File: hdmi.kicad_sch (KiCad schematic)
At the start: 25 parts, among them J3 HDMI_A, U3 TFP410PAP, U5 PCA9306, U6 TPS2041B

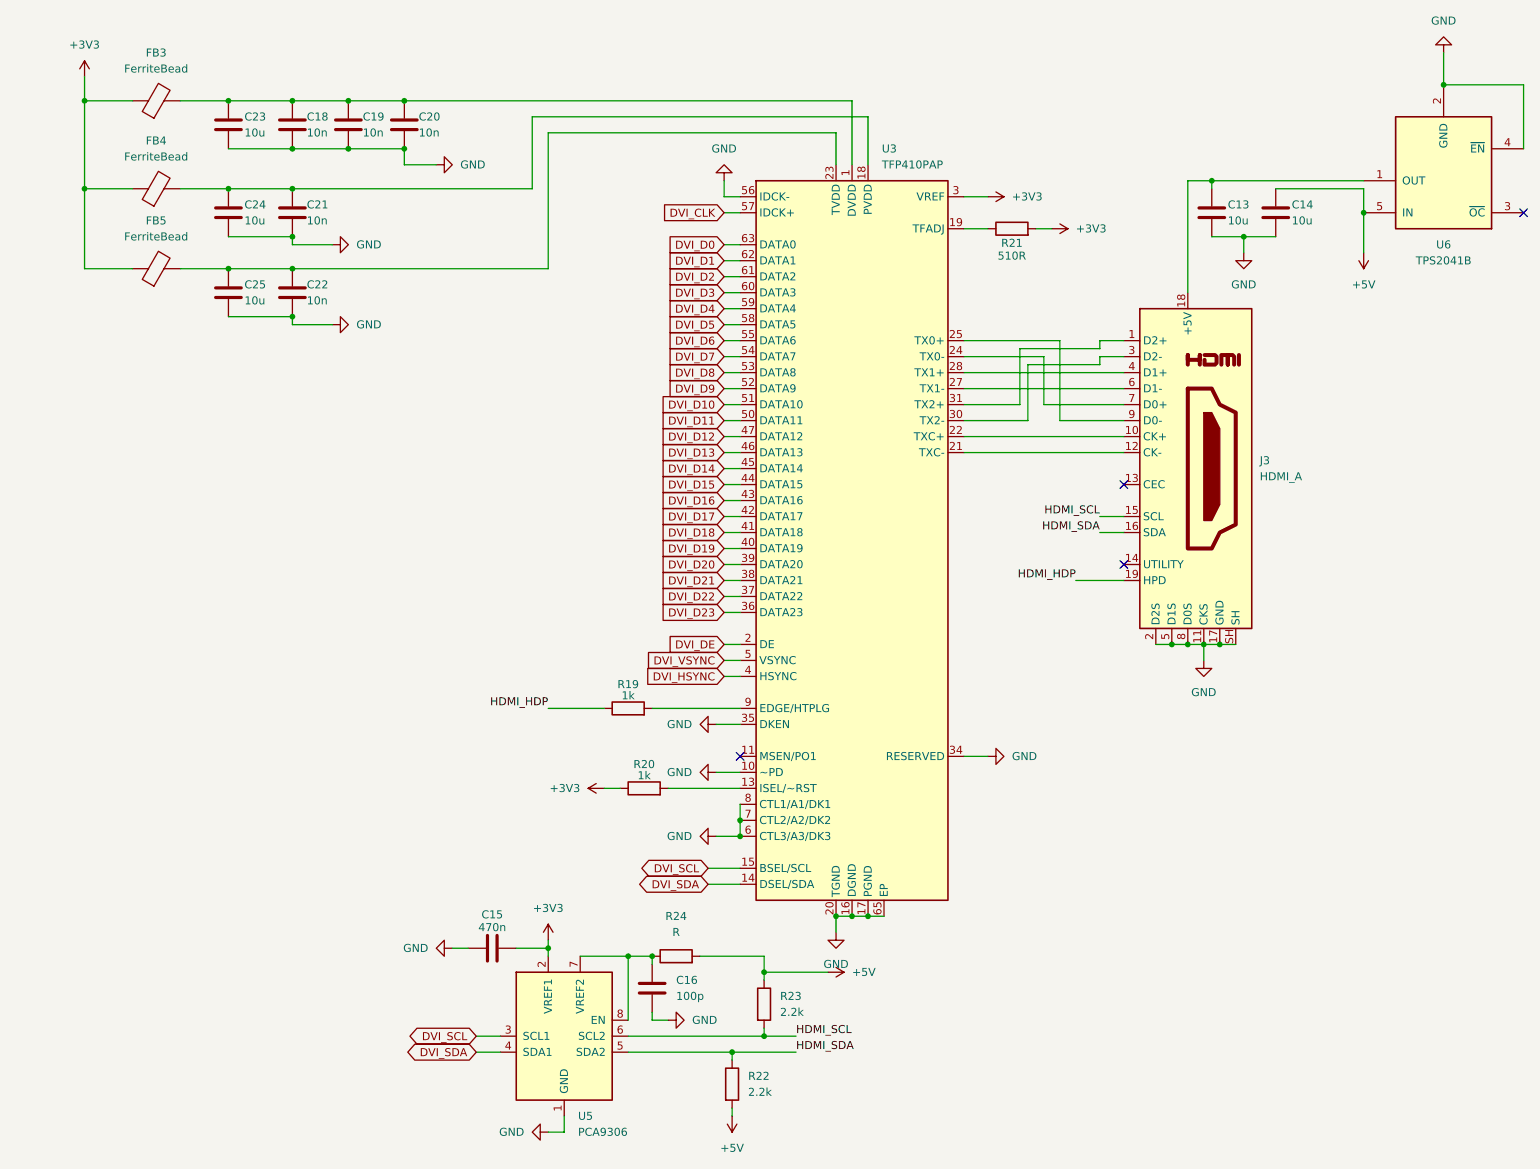
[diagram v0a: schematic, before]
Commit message: Adicionando novos datasheets e comecando power
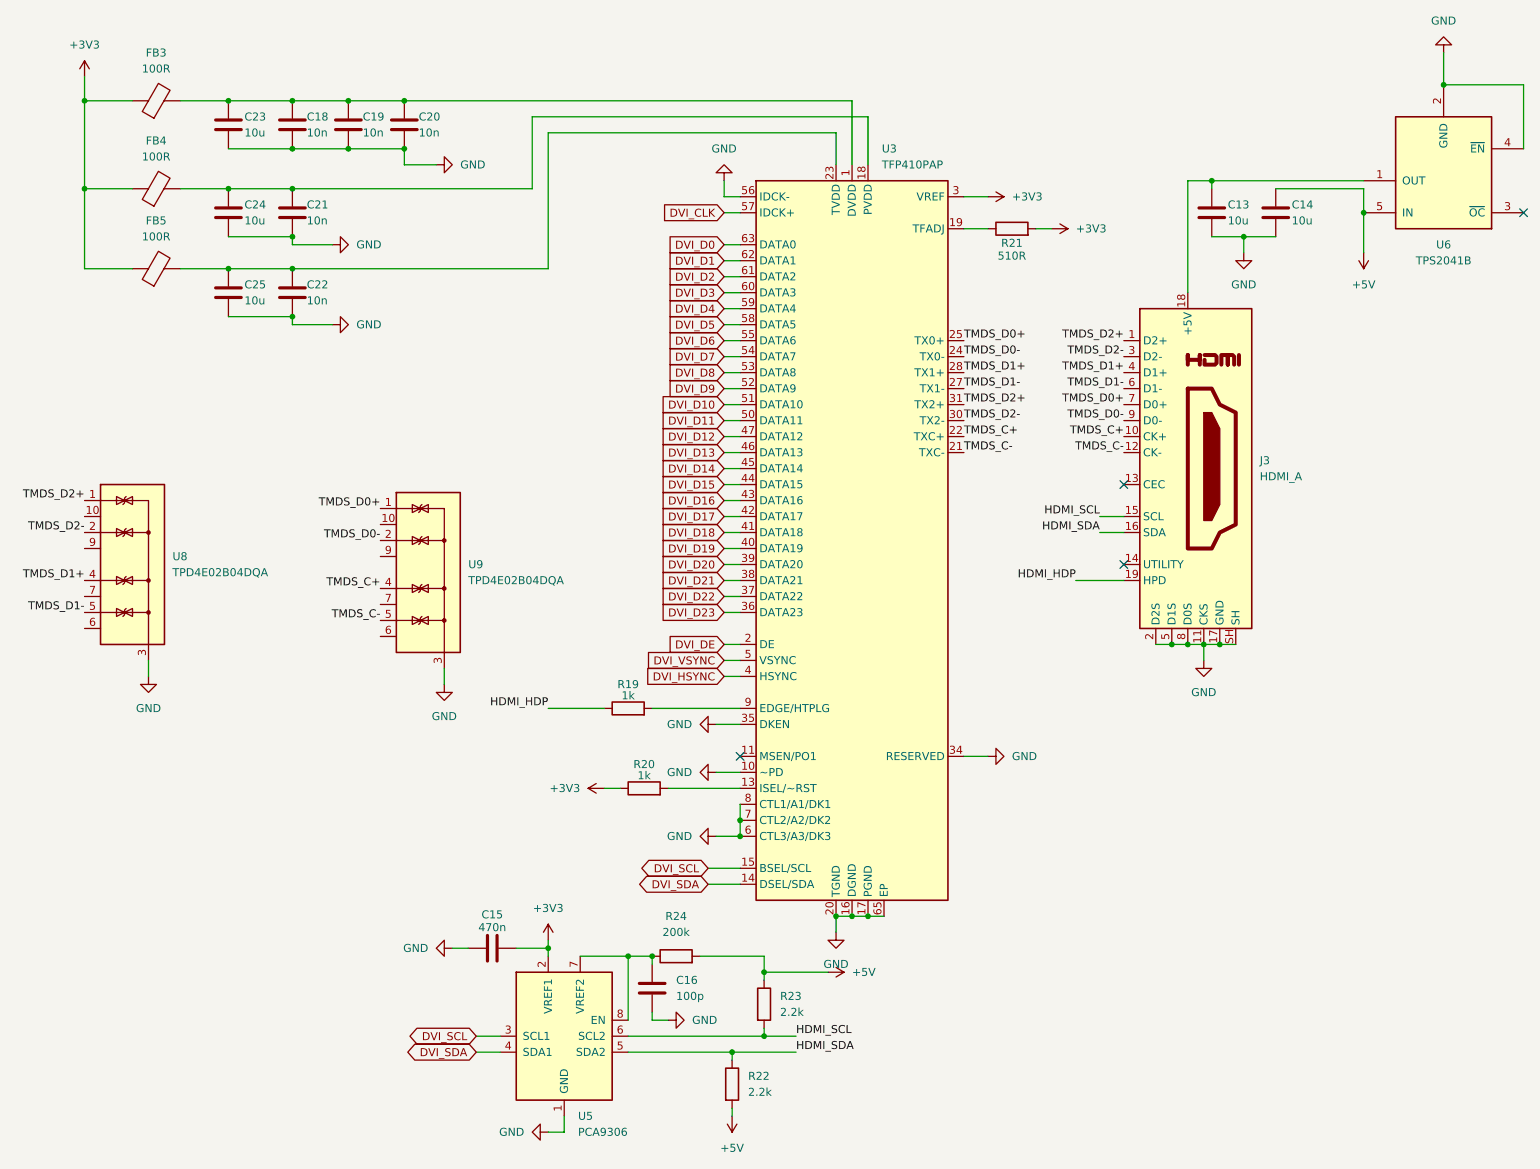
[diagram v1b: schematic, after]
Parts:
- added U8, U9: TPD4E02B04DQA, Package_SON:USON-10_2.5x1.0mm_P0.5mm, symbol Power_Protection:TPD4E02B04DQA
- FB3, FB4, FB5: value FerriteBead -> 100R
- R24: value R -> 200k
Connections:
- net GND: now also U8.3 (G), U8.8 (G), U9.3 (G), U9.8 (G)
- net TMDS_D2+: now reaches J3.1 (D2+), U3.31 (TX2+)
- net TMDS_D2+: now also U8.1 (IO1)
- net TMDS_C+: now reaches J3.10 (CK+), U3.22 (TXC+)
- net TMDS_C+: now also U9.4 (IO3)
- net TMDS_C-: now reaches J3.12 (CK-), U3.21 (TXC-)
- net TMDS_C-: now also U9.5 (IO4)
- net TMDS_D2-: now reaches J3.3 (D2-), U3.30 (TX2-)
- net TMDS_D2-: now also U8.2 (IO2)
- net TMDS_D1+: now reaches J3.4 (D1+), U3.28 (TX1+)
- net TMDS_D1+: now also U8.4 (IO3)
- net TMDS_D1-: now reaches J3.6 (D1-), U3.27 (TX1-)
- net TMDS_D1-: now also U8.5 (IO4)
- net TMDS_D0+: now reaches J3.7 (D0+)
- net TMDS_D0+: now also U3.25 (TX0+), U9.1 (IO1); no longer U3.24 (TX0-)
- net TMDS_D0-: now reaches J3.9 (D0-)
- net TMDS_D0-: now also U3.24 (TX0-), U9.2 (IO2); no longer U3.25 (TX0+)
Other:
- title: ECP5 85F Platonic Board -> PatchLogic 85 FPGA Board
